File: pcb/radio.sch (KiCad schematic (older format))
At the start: 0 parts

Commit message: Added radio circuit
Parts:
- added C1, C2, C3, C4, C5, C6: C, symbol C
- added C?: 100n, symbol C
- added C?: 100p, symbol C
- added C?: 1u, symbol C
- added IC?: Si4460, agg:QFN-20-EP-SI, symbol Si4460
- added L1, L2, L3, L4, L5, L6: L, symbol L
- added P?: COAX, agg:SMA-EDGE, symbol COAX
- added Y?: TCXO, symbol TCXO
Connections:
- new net: IC?.17 (XIN), Y?.3 (OUT)
- new net: C5.1, L4.2, P?.1 (RF)
- new net: C4.1, L3.2, L4.1
- new net: C2.2, C3.1, L2.2, L3.1, L6.1
- new net: C1.2, L2.1
- new net 3v3: C?.2, C?.2, C?.2, IC?.6 (VDD), IC?.8 (VDD), L1.1, Y?.4 (VCC)
- new net GND: C3.2, C4.2, C5.2, C6.2, C?.1, C?.1, C?.1, IC?.18 (GND), IC?.EP (GND), P?.2 (GND), Y?.2 (GND)
- new net RADIO_RXn: C2.1, IC?.3 (RXn), L5.1
- new net RADIO_RXp: C6.1, IC?.2 (RXp), L5.2, L6.2
- new net RADIO_SCLK: IC?.12 (SCLK)
- new net RADIO_SDI: IC?.14 (SDI)
- new net RADIO_SDN: IC?.1 (SDN)
- new net RADIO_SDO: IC?.13 (SDO)
- new net RADIO_TX: C1.1, IC?.4 (TX), L1.2
- new net RADIO_nIRQ: IC?.11 (nIRQ)
- new net RADIO_nSEL: IC?.15 (nSEL)
- no-connect marks 0 -> 5

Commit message: Schematic almost done.
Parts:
- gave numbers to parts that had none: 6
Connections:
- no-connect marks 5 -> 6
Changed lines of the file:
@@
 $EndDescr
 $Comp
-L Si4460 IC?
+L Si4460 IC401
 U 1 1 5A68AEFA
 P 2650 2000
-F 0 "IC?" H 2350 2700 50  0000 L CNN
+F 0 "IC401" H 2350 2700 50  0000 L CNN
 F 1 "Si4460" H 2350 1300 50  0000 L CNN
 F 2 "agg:QFN-20-EP-SI" H 2350 1200 50  0001 L CNN
@@
 	1    0    0    -1
 $EndComp
-Text Label 2100 2200 2    60   ~ 0
-RADIO_SDN
-Text Label 2100 2300 2    60   ~ 0
-RADIO_SCLK
-Text Label 2100 2400 2    60   ~ 0
-RADIO_SDO
-Text Label 2100 2500 2    60   ~ 0
-RADIO_SDI
 Wire Wire Line
 	2100 2200 2250 2200
@@
 	2100 2500 2250 2500
 $Comp
-L GND #PWR?
+L GND #PWR017
 U 1 1 5A68B038
 P 2050 1800
-F 0 "#PWR?" H 1920 1840 50  0001 L CNN
+F 0 "#PWR017" H 1920 1840 50  0001 L CNN
 F 1 "GND" H 2050 1700 50  0000 C CNN
 F 2 "" H 2050 1800 60  0000 C CNN
@@
 	1    0    0    -1
 $EndComp
-Wire Wire Line
-	1600 1700 2250 1700
 NoConn ~ 3050 1900
 NoConn ~ 3050 2000
 NoConn ~ 3050 2100
 NoConn ~ 3050 2200
-Text Label 3150 2300 0    60   ~ 0
-RADIO_nIRQ
 Wire Wire Line
 	3050 2300 3150 2300
 Text Label 3250 1600 0    60   ~ 0
 RADIO_TX
-Text Label 2100 2600 2    60   ~ 0
-RADIO_nSEL
 Wire Wire Line
 	2100 2600 2250 2600
 $Comp
-L C C?
+L C C407
 U 1 1 5A68B322
 P 1850 1600
-F 0 "C?" H 1900 1670 50  0000 C CNN
+F 0 "C407" H 1900 1670 50  0000 C CNN
 F 1 "100n" H 1900 1530 50  0000 C CNN
 F 2 "" H 1850 1600 50  0001 C CNN
@@
 $EndComp
 $Comp
-L C C?
+L C C406
 U 1 1 5A68B351
 P 1600 1600
-F 0 "C?" H 1650 1670 50  0000 C CNN
+F 0 "C406" H 1650 1670 50  0000 C CNN
 F 1 "100p" H 1650 1530 50  0000 C CNN
 F 2 "" H 1600 1600 50  0001 C CNN
@@
 $EndComp
 $Comp
-L C C?
+L C C408
 U 1 1 5A68B3B6
 P 2050 1600
-F 0 "C?" H 2100 1670 50  0000 C CNN
+F 0 "C408" H 2100 1670 50  0000 C CNN
 F 1 "1u" H 2100 1530 50  0000 C CNN
 F 2 "" H 2050 1600 50  0001 C CNN
@@
 Connection ~ 1850 1400
 $Comp
-L 3v3 #PWR?
+L 3v3 #PWR018
 U 1 1 5A68B692
 P 2050 1300
-F 0 "#PWR?" H 2050 1410 50  0001 L CNN
+F 0 "#PWR018" H 2050 1410 50  0001 L CNN
 F 1 "3v3" H 2050 1390 50  0000 C CNN
 F 2 "" H 2050 1300 60  0000 C CNN
@@
 $EndComp
 $Comp
-L TCXO Y?
+L TCXO Y401
 U 1 1 5A68B704
 P 1200 2000
-F 0 "Y?" H 1000 2100 50  0000 L CNN
+F 0 "Y401" H 1000 2100 50  0000 L CNN
 F 1 "TCXO" H 1000 1800 50  0000 L CNN
 F 2 "" H 1000 2000 50  0001 C CNN
@@
 	900  2100 900  2200
 $Comp
-L GND #PWR?
+L GND #PWR019
 U 1 1 5A68B7A2
 P 900 2200
-F 0 "#PWR?" H 770 2240 50  0001 L CNN
+F 0 "#PWR019" H 770 2240 50  0001 L CNN
 F 1 "GND" H 900 2100 50  0000 C CNN
 F 2 "" H 900 2200 60  0000 C CNN
@@
 NoConn ~ 3050 1700
 $Comp
-L COAX P?
+L COAX P401
 U 1 1 5A68BF1C
 P 8700 2200
-F 0 "P?" H 8700 2300 50  0000 C CNN
+F 0 "P401" H 8700 2300 50  0000 C CNN
 F 1 "COAX" H 8700 2050 50  0000 C CNN
 F 2 "agg:SMA-EDGE" H 8700 1990 50  0001 C CNN
@@
 Connection ~ 8150 2600
 $Comp
-L GND #PWR?
+L GND #PWR020
 U 1 1 5A68C4F8
 P 8150 2650
-F 0 "#PWR?" H 8020 2690 50  0001 L CNN
+F 0 "#PWR020" H 8020 2690 50  0001 L CNN
 F 1 "GND" H 8150 2550 50  0000 C CNN
 F 2 "" H 8150 2650 60  0000 C CNN
@@
 	6550 1600 6550 1500
 $Comp
-L 3v3 #PWR?
+L 3v3 #PWR021
 U 1 1 5A68CF2C
 P 6550 1500
-F 0 "#PWR?" H 6550 1610 50  0001 L CNN
+F 0 "#PWR021" H 6550 1610 50  0001 L CNN
 F 1 "3v3" H 6550 1590 50  0000 C CNN
 F 2 "" H 6550 1500 60  0000 C CNN
@@
 Wire Notes Line
 	500  3100 11200 3100
+NoConn ~ 2250 1900
+Text HLabel 2100 2200 0    60   Input ~ 0
+RADIO_SDN
+Text HLabel 2100 2300 0    60   Input ~ 0
+RADIO_SCLK
+Text HLabel 2100 2400 0    60   Input ~ 0
+RADIO_SDO
+Text HLabel 2100 2500 0    60   Input ~ 0
+RADIO_SDI
+Text HLabel 2100 2600 0    60   Input ~ 0
+RADIO_nSEL
+Text HLabel 3150 2300 2    60   Input ~ 0
+RADIO_nIRQ
+Wire Wire Line
+	1600 1700 2250 1700
 $EndSCHEMATC

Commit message: Attempt to fix symbol library problems from old kicad version
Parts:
- C1, C2, C3, C4, C406, C407, C408, C5, C6: symbol C -> agg-kicad:C
- IC401: symbol Si4460 -> agg-kicad:Si4460
- L1, L2, L3, L4, L5, L6: symbol L -> agg-kicad:L
- P401: symbol COAX -> agg-kicad:COAX
- Y401: symbol TCXO -> agg-kicad:TCXO
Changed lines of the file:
@@
-EESchema Schematic File Version 2
-LIBS:agg-kicad
+EESchema Schematic File Version 4
 LIBS:jerboa-cache
-EELAYER 25 0
+EELAYER 26 0
 EELAYER END
 $Descr A4 11693 8268
@@
 $EndDescr
 $Comp
-L Si4460 IC401
+L agg-kicad:Si4460 IC401
 U 1 1 5A68AEFA
 P 2650 2000
@@
 	2100 2500 2250 2500
 $Comp
-L GND #PWR017
+L agg-kicad:GND #PWR017
 U 1 1 5A68B038
 P 2050 1800
@@
 	2100 2600 2250 2600
 $Comp
-L C C407
+L agg-kicad:C C407
 U 1 1 5A68B322
 P 1850 1600
@@
 $EndComp
 $Comp
-L C C406
+L agg-kicad:C C406
 U 1 1 5A68B351
 P 1600 1600
@@
 $EndComp
 $Comp
-L C C408
+L agg-kicad:C C408
 U 1 1 5A68B3B6
 P 2050 1600
@@
 $EndComp
 Wire Wire Line
-	900  1400 2250 1400
+	900  1400 1600 1400
 Wire Wire Line
 	1850 1700 1850 1600
@@
 Connection ~ 1850 1700
 Wire Wire Line
-	2050 1600 2050 1800
+	2050 1600 2050 1700
 Wire Wire Line
 	2250 1600 2150 1600
@@
 Connection ~ 2150 1400
 Wire Wire Line
-	2050 1300 2050 1500
+	2050 1300 2050 1400
 Wire Wire Line
 	1850 1400 1850 1500
@@
 Connection ~ 1850 1400
 $Comp
-L 3v3 #PWR018
+L agg-kicad:3v3 #PWR018
 U 1 1 5A68B692
 P 2050 1300
@@
 $EndComp
 $Comp
-L TCXO Y401
+L agg-kicad:TCXO Y401
 U 1 1 5A68B704
 P 1200 2000
@@
 	900  2100 900  2200
 $Comp
-L GND #PWR019
+L agg-kicad:GND #PWR019
 U 1 1 5A68B7A2
 P 900 2200
@@
 NoConn ~ 3050 1700
 $Comp
-L COAX P401
+L agg-kicad:COAX P401
 U 1 1 5A68BF1C
 P 8700 2200
@@
 $EndComp
 $Comp
-L C C5
+L agg-kicad:C C5
 U 1 1 5A68C1A2
 P 8150 2350
@@
 $EndComp
 $Comp
-L C C4
+L agg-kicad:C C4
 U 1 1 5A68C1D3
 P 7750 2350
@@
 $EndComp
 $Comp
-L C C3
+L agg-kicad:C C3
 U 1 1 5A68C21E
 P 7350 2350
@@
 $EndComp
 $Comp
-L L L3
+L agg-kicad:L L3
 U 1 1 5A68C28F
 P 7500 2200
@@
 $EndComp
 $Comp
-L L L4
+L agg-kicad:L L4
 U 1 1 5A68C2C2
 P 7900 2200
@@
 	8150 2200 8150 2350
 Wire Wire Line
-	8150 2450 8150 2650
+	8150 2450 8150 2600
 Wire Wire Line
 	7750 2600 7750 2450
@@
 Connection ~ 8150 2600
 $Comp
-L GND #PWR020
+L agg-kicad:GND #PWR020
 U 1 1 5A68C4F8
 P 8150 2650
@@
 Connection ~ 7350 2200
 $Comp
-L L L2
+L agg-kicad:L L2
 U 1 1 5A68C669
 P 7100 1850
@@
 $EndComp
 $Comp
-L C C1
+L agg-kicad:C C1
 U 1 1 5A68C69E
 P 6700 1850
@@
 $EndComp
 $Comp
-L C C2
+L agg-kicad:C C2
 U 1 1 5A68C6CF
 P 6700 2200
@@
 RADIO_TX
 $Comp
-L L L1
+L agg-kicad:L L1
 U 1 1 5A68C86D
 P 6550 1600
@@
 	6550 1600 6550 1500
 $Comp
-L 3v3 #PWR021
+L agg-kicad:3v3 #PWR021
 U 1 1 5A68CF2C
 P 6550 1500
@@
 $EndComp
 $Comp
-L L L6
+L agg-kicad:L L6
 U 1 1 5A68D25F
 P 6950 2350
@@
 $EndComp
 $Comp
-L L L5
+L agg-kicad:L L5
 U 1 1 5A68D2B8
 P 6550 2350
@@
 Connection ~ 6950 2600
 Wire Wire Line
-	8000 2200 8600 2200
-Wire Wire Line
-	7600 2200 7900 2200
+	8000 2200 8150 2200
+Wire Wire Line
+	7600 2200 7750 2200
 Wire Wire Line
 	7350 1850 7200 1850
-Connection ~ 6950 1850
 Wire Wire Line
 	8600 2300 8600 2600
 Connection ~ 8150 2200
 $Comp
-L C C6
+L agg-kicad:C C6
 U 1 1 5A68EAFA
 P 7100 2600
@@
 $EndComp
 Wire Wire Line
-	6800 2200 7500 2200
+	6800 2200 6950 2200
 Wire Wire Line
 	6950 2350 6950 2200
 Wire Wire Line
-	6400 2600 7100 2600
-Wire Wire Line
-	6400 2200 6700 2200
-Wire Wire Line
-	8600 2600 7200 2600
-Wire Wire Line
-	6800 1850 7100 1850
+	6400 2600 6550 2600
+Wire Wire Line
+	6400 2200 6550 2200
+Wire Wire Line
+	8600 2600 8150 2600
 Wire Wire Line
 	6550 1700 6550 1850
 Wire Wire Line
-	6400 1850 6700 1850
-Wire Wire Line
-	7350 1850 7350 2350
+	6400 1850 6550 1850
+Wire Wire Line
+	7350 1850 7350 2200
 Connection ~ 6550 2200
 Connection ~ 6550 2600
@@
 RADIO_nIRQ
 Wire Wire Line
-	1600 1700 2250 1700
+	1600 1700 1850 1700
+Wire Wire Line
+	2050 1700 2050 1800
+Wire Wire Line
+	2050 1700 2150 1700
+Wire Wire Line
+	1850 1700 2050 1700
+Wire Wire Line
+	2150 1700 2250 1700
+Wire Wire Line
+	2150 1400 2250 1400
+Wire Wire Line
+	2050 1400 2150 1400
+Wire Wire Line
+	2050 1400 2050 1500
+Wire Wire Line
+	1850 1400 2050 1400
+Wire Wire Line
+	1600 1400 1850 1400
+Wire Wire Line
+	7750 2600 7350 2600
+Wire Wire Line
+	7750 2200 7900 2200
+Wire Wire Line
+	8150 2600 8150 2650
+Wire Wire Line
+	8150 2600 7750 2600
+Wire Wire Line
+	7350 2200 7500 2200
+Wire Wire Line
+	7350 2200 7350 2350
+Wire Wire Line
+	6550 1850 6700 1850
+Wire Wire Line
+	6950 2200 7350 2200
+Wire Wire Line
+	7350 2600 7200 2600
+Wire Wire Line
+	6950 2600 7100 2600
+Wire Wire Line
+	8150 2200 8600 2200
+Wire Wire Line
+	6550 2200 6700 2200
+Wire Wire Line
+	6550 2600 6950 2600
+Wire Wire Line
+	6800 1850 7100 1850
 $EndSCHEMATC

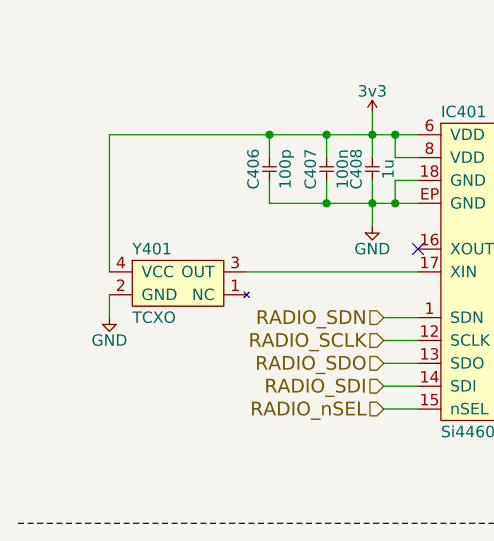
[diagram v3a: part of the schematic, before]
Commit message: Some schematic work, create a todo with ideas for power supply components
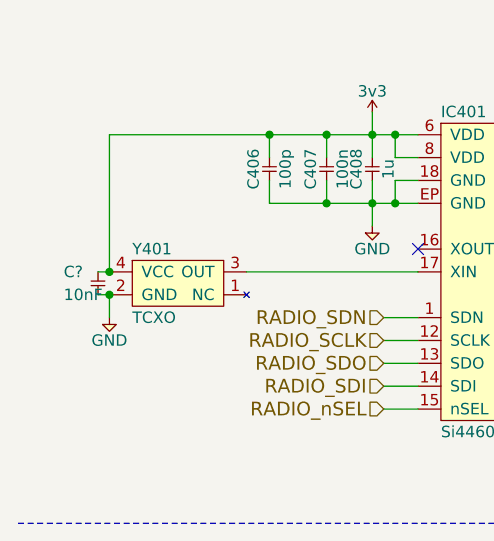
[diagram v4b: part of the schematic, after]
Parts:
- added C?: 10nF, agg:0402, symbol agg-kicad:C
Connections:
- net 3v3: now also C?.1
- net GND: now also C?.2
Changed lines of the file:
@@
 Wire Wire Line
 	6800 1850 7100 1850
+$Comp
+L agg-kicad:C C?
+U 1 1 5A700303
+P 850 2000
+F 0 "C?" V 850 1850 50  0000 L CNN
+F 1 "10nF" V 950 1850 50  0000 L CNN
+F 2 "agg:0402" H 850 2000 50  0001 C CNN
+F 3 "" H 850 2000 50  0001 C CNN
+F 4 "1414575" H 850 2000 50  0001 C CNN "Farnell"
+	1    850  2000
+	0    1    1    0
+$EndComp
+Wire Wire Line
+	850  2000 900  2000
+Connection ~ 900  2000
+Wire Wire Line
+	850  2100 900  2100
+Connection ~ 900  2100
 $EndSCHEMATC

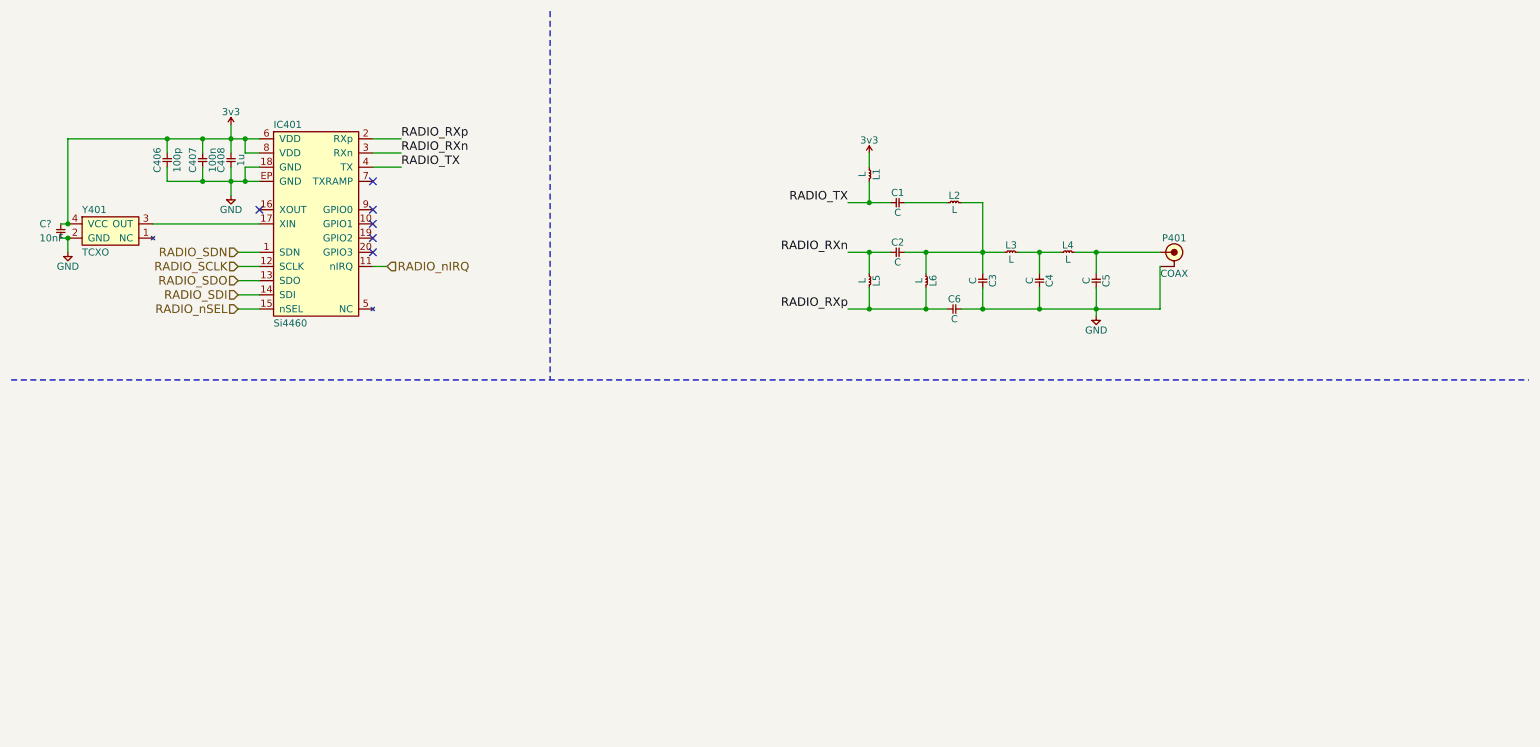
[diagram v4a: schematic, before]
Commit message: Create some more schematic symbols and footprints
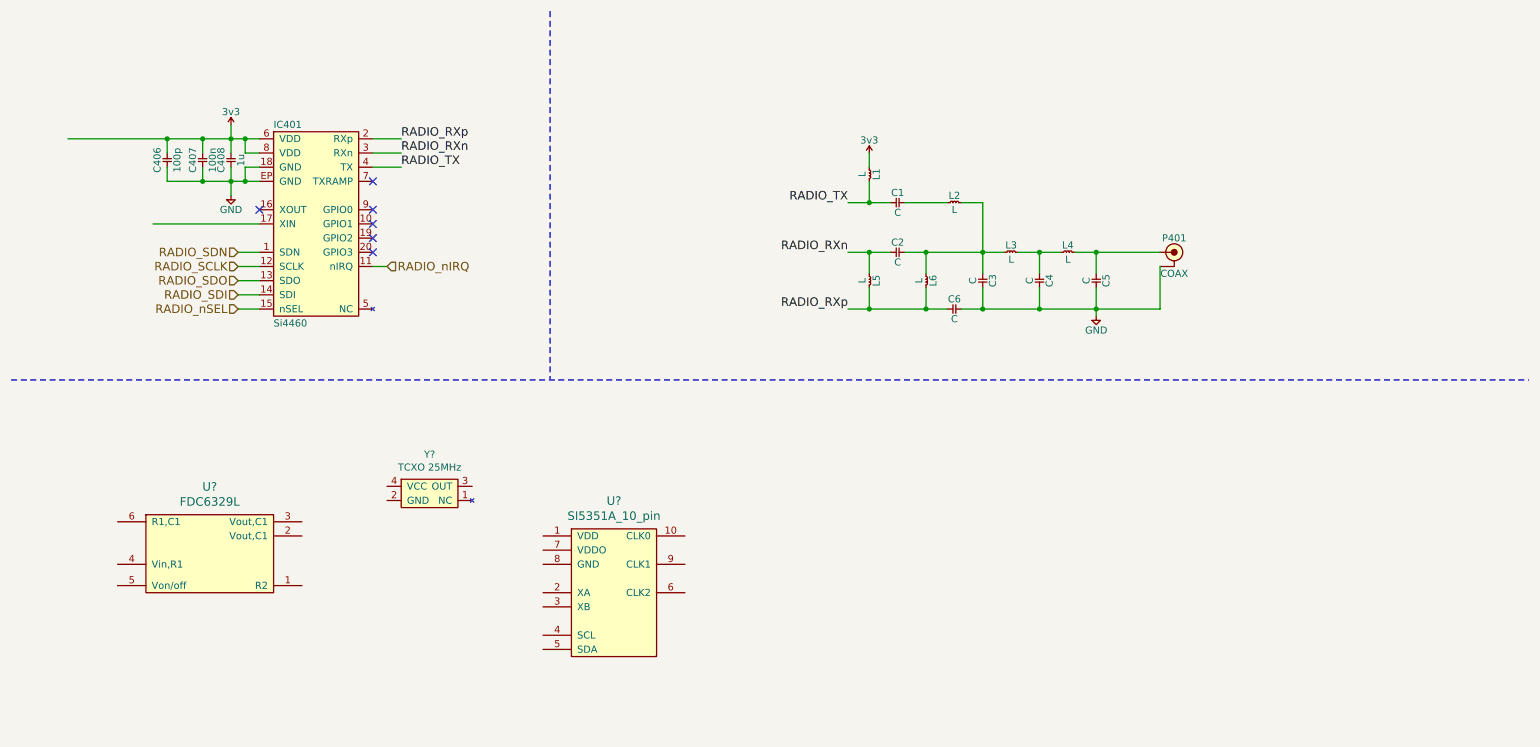
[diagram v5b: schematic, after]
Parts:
- removed C?: 10nF, agg:0402, symbol agg-kicad:C
- removed Y401: TCXO, symbol agg-kicad:TCXO
- added U?: SI5351A_10_pin, symbol SI5351A_10_pin:SI5351A_10_pin
- added U?: FDC6329L, Jerboa:SuperSOT-6, symbol FDC6329L:FDC6329L
- added Y?: TCXO 25MHz, Jerboa:ASTX_H11, symbol agg-kicad:TCXO
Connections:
- wire segments 70 -> 44
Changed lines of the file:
@@
 $EndComp
 Wire Wire Line
-	900  1400 1600 1400
+	900  1400 2250 1400
 Wire Wire Line
 	1850 1700 1850 1600
@@
 Connection ~ 1850 1700
 Wire Wire Line
-	2050 1600 2050 1700
+	2050 1600 2050 1800
 Wire Wire Line
 	2250 1600 2150 1600
@@
 Connection ~ 2150 1400
 Wire Wire Line
-	2050 1300 2050 1400
+	2050 1300 2050 1500
 Wire Wire Line
 	1850 1400 1850 1500
@@
 	1    0    0    -1
 $EndComp
-$Comp
-L agg-kicad:TCXO Y401
-U 1 1 5A68B704
-P 1200 2000
-F 0 "Y401" H 1000 2100 50  0000 L CNN
-F 1 "TCXO" H 1000 1800 50  0000 L CNN
-F 2 "" H 1000 2000 50  0001 C CNN
-F 3 "" H 1000 2000 50  0001 C CNN
-F 4 "2405785" H 1000 1700 50  0001 L CNN "Farnell"
-	1    1200 2000
-	1    0    0    -1
-$EndComp
-Wire Wire Line
-	900  1400 900  2000
 Connection ~ 1600 1400
-Wire Wire Line
-	900  2100 900  2200
-$Comp
-L agg-kicad:GND #PWR019
-U 1 1 5A68B7A2
-P 900 2200
-F 0 "#PWR019" H 770 2240 50  0001 L CNN
-F 1 "GND" H 900 2100 50  0000 C CNN
-F 2 "" H 900 2200 60  0000 C CNN
-F 3 "" H 900 2200 60  0000 C CNN
-	1    900  2200
-	1    0    0    -1
-$EndComp
 Wire Wire Line
 	1500 2000 2250 2000
@@
 	8150 2200 8150 2350
 Wire Wire Line
-	8150 2450 8150 2600
+	8150 2450 8150 2650
 Wire Wire Line
 	7750 2600 7750 2450
@@
 Connection ~ 6950 2600
 Wire Wire Line
-	8000 2200 8150 2200
-Wire Wire Line
-	7600 2200 7750 2200
+	8000 2200 8600 2200
+Wire Wire Line
+	7600 2200 7900 2200
 Wire Wire Line
 	7350 1850 7200 1850
@@
 $EndComp
 Wire Wire Line
-	6800 2200 6950 2200
+	6800 2200 7500 2200
 Wire Wire Line
 	6950 2350 6950 2200
 Wire Wire Line
-	6400 2600 6550 2600
-Wire Wire Line
-	6400 2200 6550 2200
-Wire Wire Line
-	8600 2600 8150 2600
+	6400 2600 7100 2600
+Wire Wire Line
+	6400 2200 6700 2200
+Wire Wire Line
+	7200 2600 8600 2600
 Wire Wire Line
 	6550 1700 6550 1850
 Wire Wire Line
-	6400 1850 6550 1850
-Wire Wire Line
-	7350 1850 7350 2200
+	6400 1850 6700 1850
+Wire Wire Line
+	7350 1850 7350 2350
 Connection ~ 6550 2200
 Connection ~ 6550 2600
@@
 RADIO_nIRQ
 Wire Wire Line
-	1600 1700 1850 1700
-Wire Wire Line
-	2050 1700 2050 1800
-Wire Wire Line
-	2050 1700 2150 1700
-Wire Wire Line
-	1850 1700 2050 1700
-Wire Wire Line
-	2150 1700 2250 1700
-Wire Wire Line
-	2150 1400 2250 1400
-Wire Wire Line
-	2050 1400 2150 1400
-Wire Wire Line
-	2050 1400 2050 1500
-Wire Wire Line
-	1850 1400 2050 1400
-Wire Wire Line
-	1600 1400 1850 1400
-Wire Wire Line
-	7750 2600 7350 2600
-Wire Wire Line
-	7750 2200 7900 2200
-Wire Wire Line
-	8150 2600 8150 2650
-Wire Wire Line
-	8150 2600 7750 2600
-Wire Wire Line
-	7350 2200 7500 2200
-Wire Wire Line
-	7350 2200 7350 2350
-Wire Wire Line
-	6550 1850 6700 1850
-Wire Wire Line
-	6950 2200 7350 2200
-Wire Wire Line
-	7350 2600 7200 2600
-Wire Wire Line
-	6950 2600 7100 2600
-Wire Wire Line
-	8150 2200 8600 2200
-Wire Wire Line
-	6550 2200 6700 2200
-Wire Wire Line
-	6550 2600 6950 2600
+	1600 1700 2250 1700
 Wire Wire Line
 	6800 1850 7100 1850
 $Comp
-L agg-kicad:C C?
-U 1 1 5A700303
-P 850 2000
-F 0 "C?" V 850 1850 50  0000 L CNN
-F 1 "10nF" V 950 1850 50  0000 L CNN
-F 2 "agg:0402" H 850 2000 50  0001 C CNN
-F 3 "" H 850 2000 50  0001 C CNN
-F 4 "1414575" H 850 2000 50  0001 C CNN "Farnell"
-	1    850  2000
-	0    1    1    0
-$EndComp
-Wire Wire Line
-	850  2000 900  2000
-Connection ~ 900  2000
-Wire Wire Line
-	850  2100 900  2100
-Connection ~ 900  2100
+L agg-kicad:TCXO Y?
+U 1 1 5A7CB0D5
+P 3450 3850
+F 0 "Y?" H 3450 4075 50  0000 C CNN
+F 1 "TCXO 25MHz" H 3450 3984 50  0000 C CNN
+F 2 "Jerboa:ASTX_H11" H 3250 3850 50  0001 C CNN
+F 3 "" H 3250 3850 50  0001 C CNN
+F 4 "535-12039-1-ND" H 3450 3850 60  0001 C CNN "Digikey"
+	1    3450 3850
+	1    0    0    -1
+$EndComp
+$Comp
+L SI5351A_10_pin:SI5351A_10_pin U?
+U 1 1 5A7CC074
+P 4250 4200
+F 0 "U?" H 4750 4447 60  0000 C CNN
+F 1 "SI5351A_10_pin" H 4750 4341 60  0000 C CNN
+F 2 "" H 4250 4200 60  0001 C CNN
+F 3 "" H 4250 4200 60  0001 C CNN
+	1    4250 4200
+	1    0    0    -1
+$EndComp
+$Comp
+L FDC6329L:FDC6329L U?
+U 1 1 5A7E3431
+P 1900 4200
+F 0 "U?" H 1900 4547 60  0000 C CNN
+F 1 "FDC6329L" H 1900 4441 60  0000 C CNN
+F 2 "Jerboa:SuperSOT-6" H 1900 3550 60  0001 C CNN
+F 3 "http://www.farnell.com/datasheets/2285836.pdf" H 1900 3650 60  0001 C CNN
+F 4 "1652469" H 1900 3450 60  0001 C CNN "Farnell"
+	1    1900 4200
+	1    0    0    -1
+$EndComp
 $EndSCHEMATC
